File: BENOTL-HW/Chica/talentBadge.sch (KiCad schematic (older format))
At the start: 62 parts, among them P1 USB_A, P2 OLED, P3 Batt, P4 PS, P5 sd_card_spi, Q1 MMBT3904, Q2 MMBT3904, Q3 IR phototransistor, SW1 B1, SW2 B2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

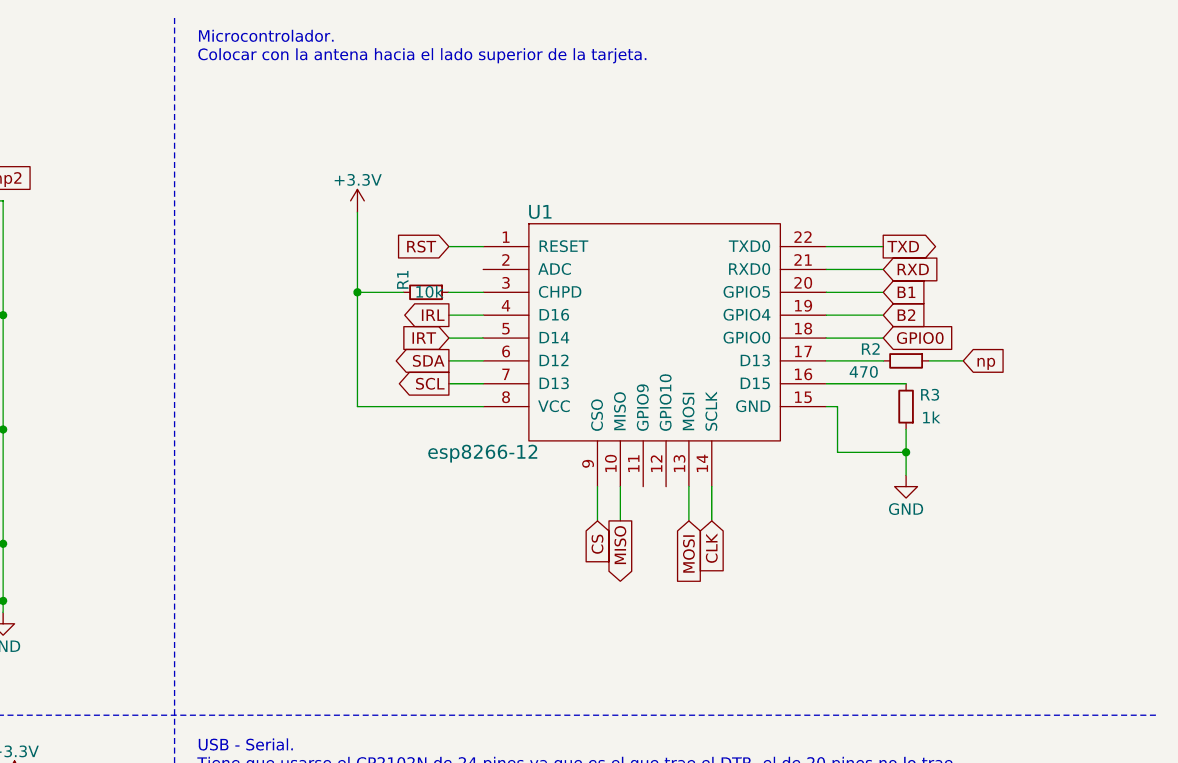
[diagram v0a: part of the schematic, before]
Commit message: Add resistor to GPIO2
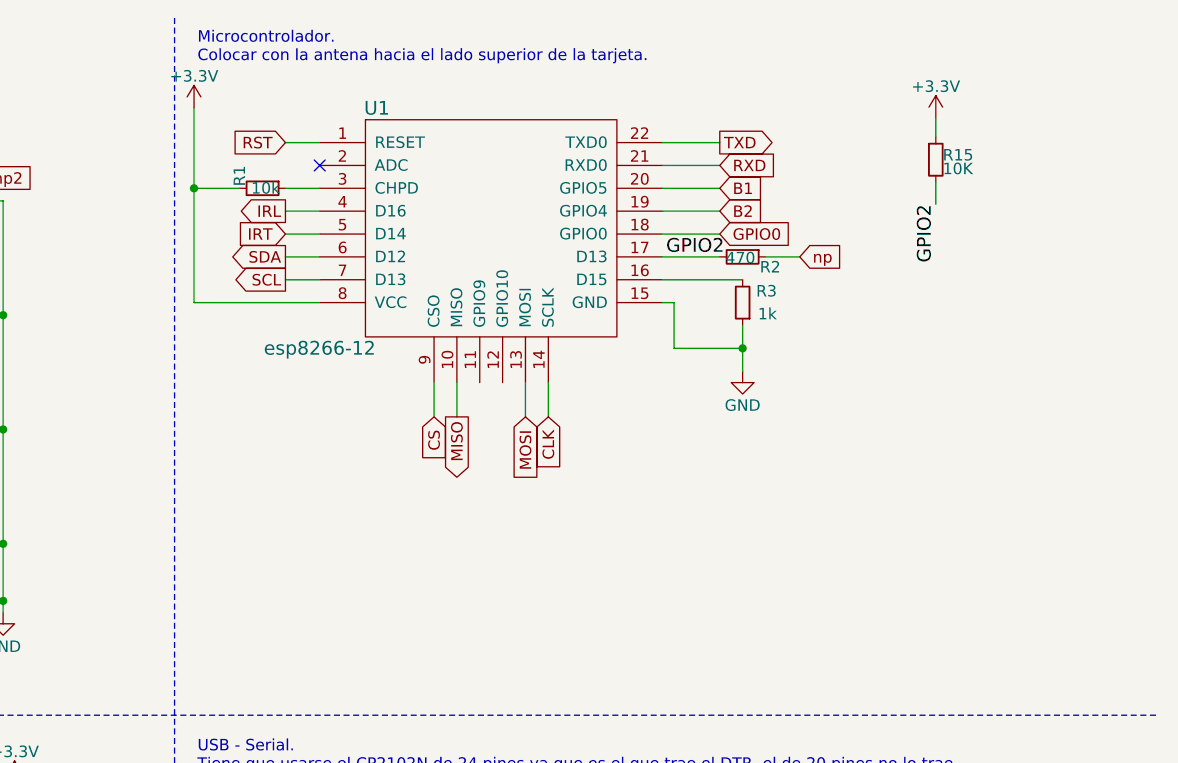
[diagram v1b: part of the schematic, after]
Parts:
- added R15: 10K, symbol R_Small
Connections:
- net +3V3: now also R15.1
- net GPIO2: now reaches R2.2, U1.17 (D13)
- net GPIO2: now also R15.2
- no-connect marks 8 -> 9
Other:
- moved on the sheet: R1, R2, R3, U1
